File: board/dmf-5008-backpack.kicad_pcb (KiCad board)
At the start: 2 copper layers, 82 x 74 mm, 66 parts, among them J1 5V IN, J2 3V3 IN, J3 BOOST, J4 Barrel_Jack_Switch, J5 CONN_SPI, J6 CONN_I2C, J7 CONN_UART, P1 CONN_01X25, Q1 BSS138, Q10 BSS138, Q11 BSS138, Q12 BSS138, Q13 BSS138, Q14 BSS138, Q2 BSS138, Q3 BSS138, Q4 BSS138, Q5 BSS138, Q6 BSS138, Q7 BSS138, Q8 BSS138, Q9 BSS138, SW1 RESET, U1 Pico, U2 MIC4830

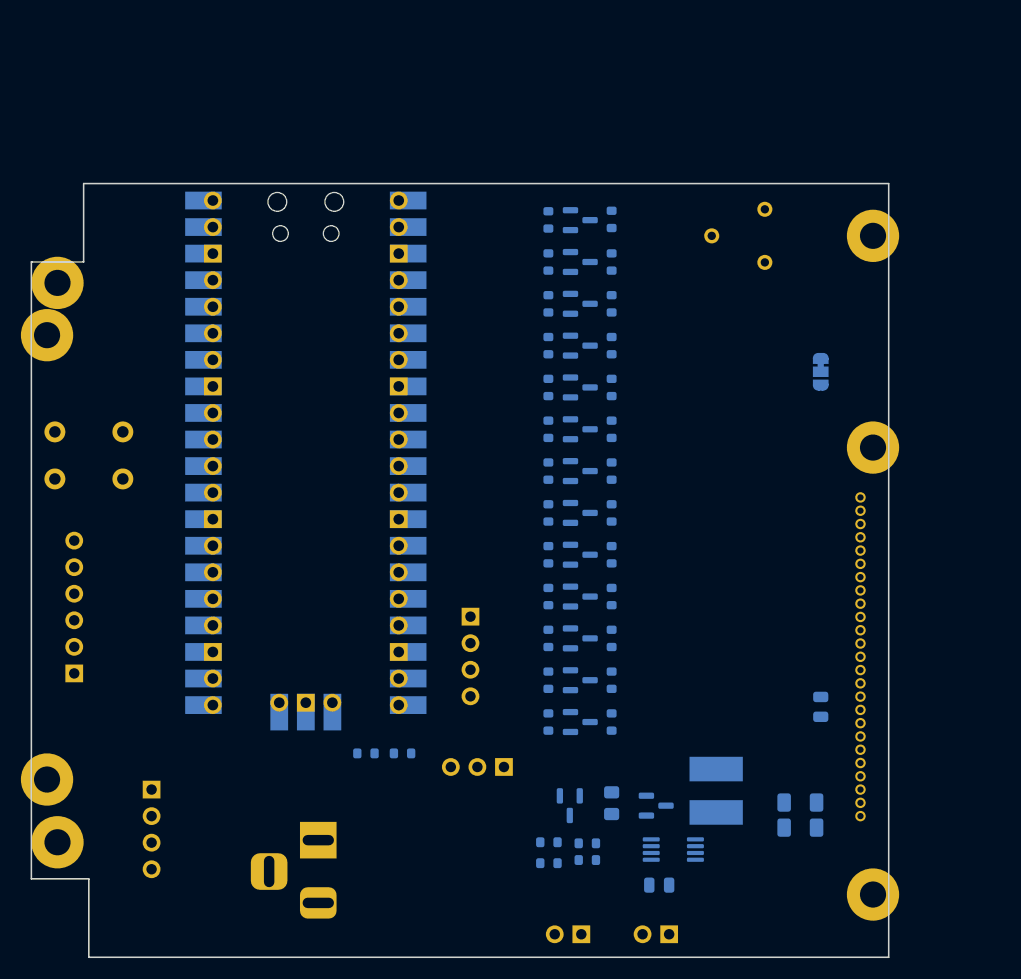
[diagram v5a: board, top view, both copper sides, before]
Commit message: PCB finished except for final checking
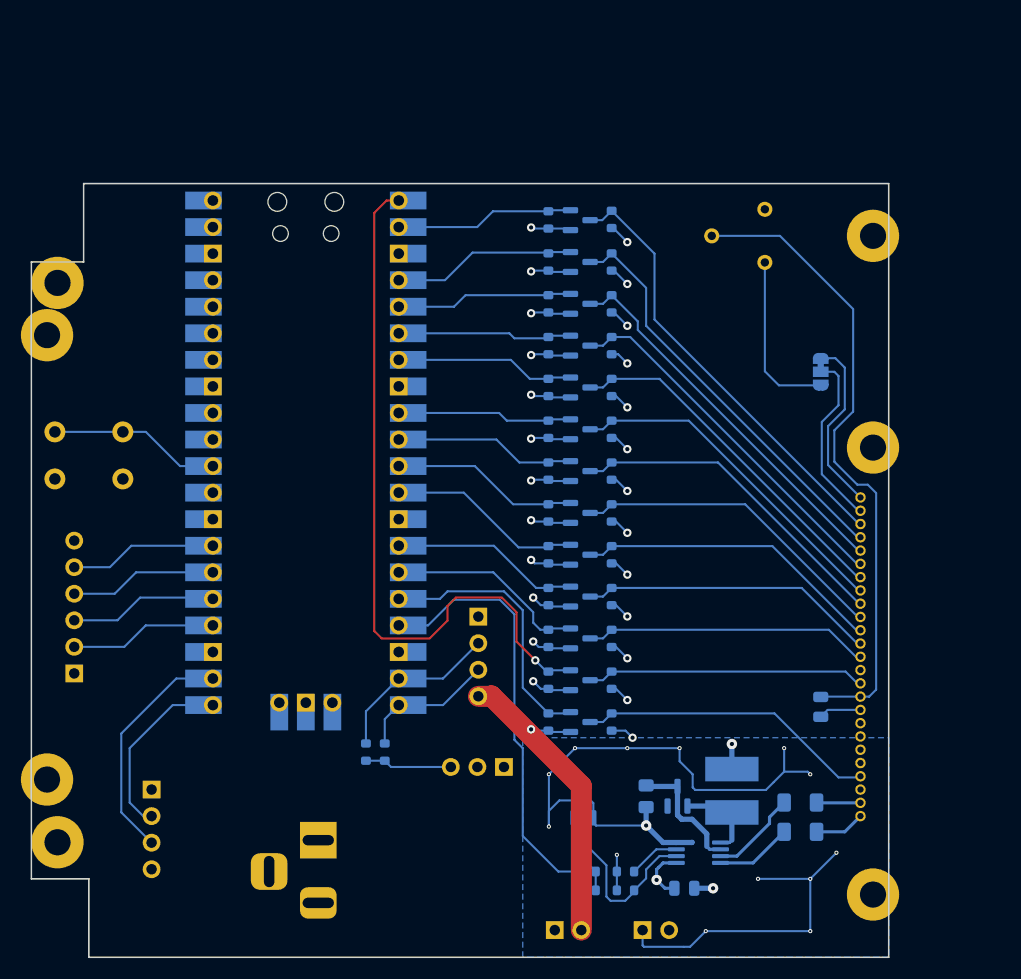
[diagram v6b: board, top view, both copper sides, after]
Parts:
- added SYM1: SYM_Flash_Large, Symbol:Symbol_Highvoltage_Type2_CopperTop_Small, B.Cu at (173.5, 130.5)
- added SYM2: Fiducial, Symbol:Symbol_Barrel_Polarity, B.Cu at (130.5, 119.5)
- moved J2 10.9 mm to (153.1, 132.4), turned to -90 degrees
- moved J1 5.87 mm to (161.5, 132.4), turned to -90 degrees
- moved R33 5.87 mm to (156.2, 128.6)
- moved R18 4.66 mm to (159.8, 128.6), turned to 0 degrees
- moved R17 4.54 mm to (159.8, 126.8)
- moved R34 3.74 mm to (156.2, 126.8)
- moved R32 3.50 mm to (135.0, 115.4), turned to 90 degrees
- moved C3 3.37 mm to (161.8, 119.6)
- moved Q9 2.47 mm to (155.8, 122.6)
- moved U2 2.42 mm to (166.8, 125.0)
- moved C2 2.42 mm to (165.4, 128.4)
- moved D1 2.23 mm to (164.8, 119.6), turned to 90 degrees
- moved R31 1.80 mm to (136.8, 115.4), turned to 90 degrees
- moved L1 1.50 mm to (170.0, 119.1)
- moved J6 0.75 mm to (145.8, 102.4)
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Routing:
- net +5V: track 0.00 -> 177.3 mm, vias 0 -> 16
- net GND: track 0.00 -> 114.9 mm, vias 0 -> 14
- net +3V3: track 0.00 -> 100.4 mm, vias 0 -> 13
- net /LCD_CS: track 0.00 -> 68.9 mm, vias 0 -> 1
- net /V0: track 0.00 -> 61.4 mm
- net /LCD_5V_A0: track 0.00 -> 42.3 mm
- net /EL_ENABLE: track 0.00 -> 40.9 mm
- net /LCD_5V_WR: track 0.00 -> 39.6 mm
- net /LCD_5V_RD: track 0.00 -> 36.8 mm
- net /LCD_5V_D0: track 0.00 -> 35.2 mm
- net /LCD_5V_D1: track 0.00 -> 34.1 mm
- net /LCD_5V_D2: track 0.00 -> 32.9 mm
- net /LCD_5V_D3: track 0.00 -> 31.8 mm
- net /LCD_5V_D4: track 0.00 -> 30.7 mm
- net /LCD_5V_D5: track 0.00 -> 29.5 mm
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- added copper zone on In1.Cu, net +3V3
- added copper zone on In1.Cu, net +5V
- added copper zone on B.Cu, net GND
- added copper zone on In2.Cu, net GND
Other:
- copper layers 2 -> 4
- board text added: "+ -"
- board text added: "+5V IN"
- board text added: "- +"
- board text added: "8080 MODE 6800"
- board text added: "90V AC"
- board text added: "DMF5008 BACKPACK DAVID TURNER JAN 2023 REVISION 1"
- board text added: "I2C: GND SDA SCL 3V3"
- board text added: "SPI: 3V3 CS MOSI MISO CLK GND"
- board text added: "UART: GND TX RX 3V3"

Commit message: Final checks and fixes
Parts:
- RV1: footprint Potentiometer_THT:Potentiometer_Bourns_3386F_Vertical -> Potentiometer_THT:Potentiometer_ACP_CA9-V10_Vertical
- moved RV1 0.93 mm to (173.8, 69.2)
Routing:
- net GND: track 114.9 -> 129.7 mm, vias 14 -> 15
- net +3V3: track 100.4 -> 106.3 mm
- net /V0: track 61.4 -> 65.4 mm
- net +5V: track 177.3 -> 175.3 mm
- net /LCD_5V_A0: track 42.3 -> 43.1 mm
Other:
- rule pad_to_mask_clearance: 0.2 -> 0
